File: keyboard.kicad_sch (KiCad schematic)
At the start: 1 part

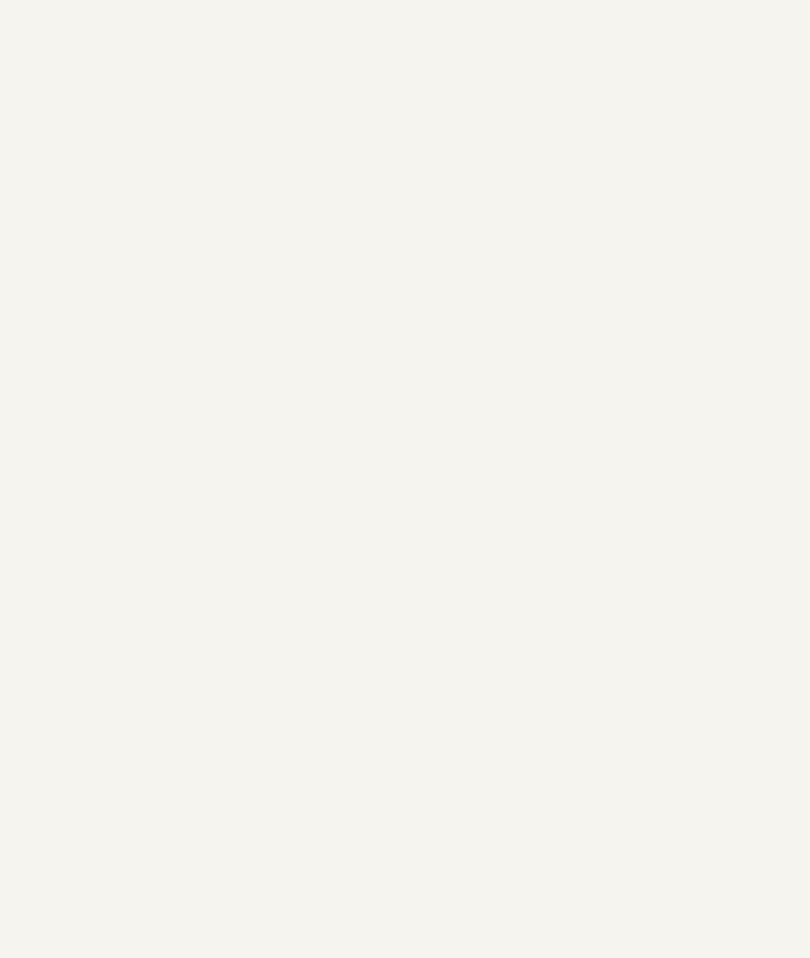
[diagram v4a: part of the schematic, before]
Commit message: added new stm uc
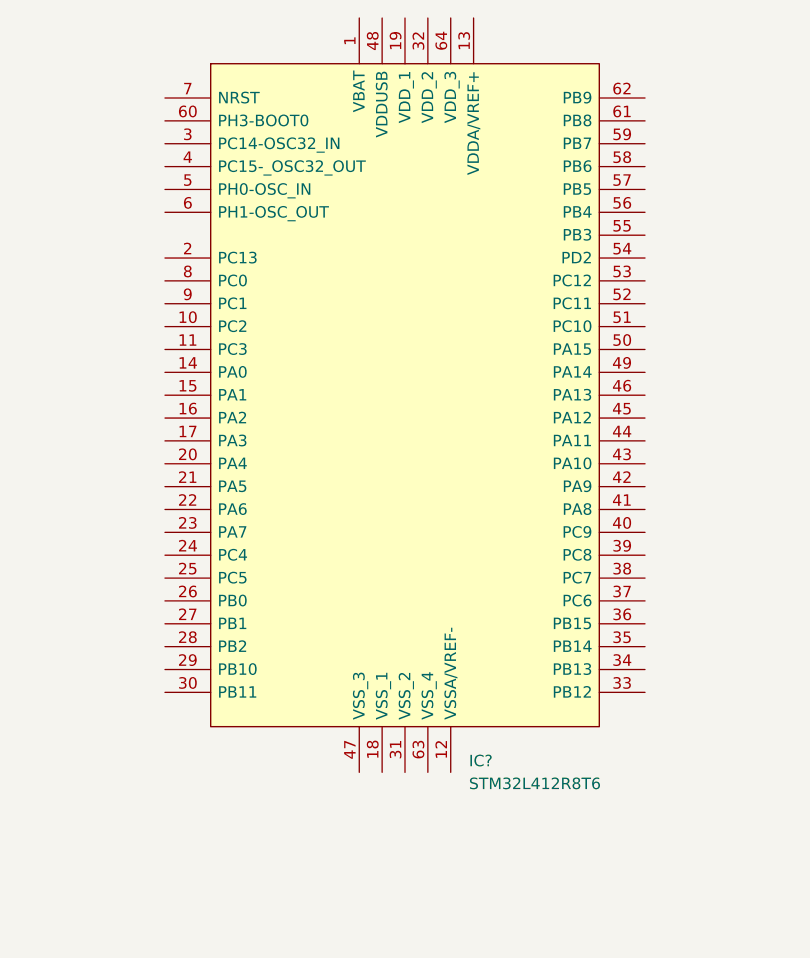
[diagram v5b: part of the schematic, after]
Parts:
- added IC?: STM32L412R8T6, CustomKeyboard:QFP50P1200X1200X160-64N, symbol CustomKeyboard:STM32L412R8T6
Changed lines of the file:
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@@
     (pin "1")
+  )
+  (symbol (lib_id "CustomKeyboard:STM32L412R8T6") (at 116.84 -74.93 0) (unit 1)
+    (in_bom yes) (on_board yes) (fields_autoplaced)
+    (property "Reference" "IC?" (id 0) (at 150.6094 -13.97 0)
+      (effects (font (size 1.27 1.27)) (justify left))
+    )
+    (property "Value" "STM32L412R8T6" (id 1) (at 150.6094 -11.43 0)
+      (effects (font (size 1.27 1.27)) (justify left))
+    )
+    (property "Footprint" "CustomKeyboard:QFP50P1200X1200X160-64N" (id 2) (at 166.37 -86.995 0)
+      (effects (font (size 1.27 1.27)) (justify left) hide)
+    )
+    (property "Datasheet" "https://www.st.com/resource/en/datasheet/stm32l412r8.pdf" (id 3) (at 166.37 -87.63 0)
+      (effects (font (size 1.27 1.27)) (justify left) hide)
+    )
+    (property "Description" "STMICROELECTRONICS - STM32L412R8T6 - MCU, 32BIT, 80MHZ" (id 4) (at 166.37 -85.09 0)
+      (effects (font (size 1.27 1.27)) (justify left) hide)
+    )
+    (property "Height" "1.6" (id 5) (at 166.37 -79.375 0)
+      (effects (font (size 1.27 1.27)) (justify left) hide)
+    )
+    (property "Mouser Part Number" "511-STM32L412R8T6" (id 6) (at 166.37 -76.835 0)
+      (effects (font (size 1.27 1.27)) (justify left) hide)
+    )
+    (property "Mouser Price/Stock" "https://www.mouser.co.uk/ProductDetail/STMicroelectronics/STM32L412R8T6?qs=l7cgNqFNU1ir0TjKK2zizg%3D%3D" (id 7) (at 166.37 -77.47 0)
+      (effects (font (size 1.27 1.27)) (justify left) hide)
+    )
+    (property "Manufacturer_Name" "STMicroelectronics" (id 8) (at 166.37 -71.755 0)
+      (effects (font (size 1.27 1.27)) (justify left) hide)
+    )
+    (property "Manufacturer_Part_Number" "STM32L412R8T6" (id 9) (at 166.37 -69.215 0)
+      (effects (font (size 1.27 1.27)) (justify left) hide)
+    )
+    (pin "1")
+    (pin "10")
+    (pin "11")
+    (pin "12")
+    (pin "13")
+    (pin "14")
+    (pin "15")
+    (pin "16")
+    (pin "17")
+    (pin "18")
+    (pin "19")
+    (pin "2")
+    (pin "20")
+    (pin "21")
+    (pin "22")
+    (pin "23")
+    (pin "24")
+    (pin "25")
+    (pin "26")
+    (pin "27")
+    (pin "28")
+    (pin "29")
+    (pin "3")
+    (pin "30")
+    (pin "31")
+    (pin "32")
+    (pin "33")
+    (pin "34")
+    (pin "35")
+    (pin "36")
+    (pin "37")
+    (pin "38")
+    (pin "39")
+    (pin "4")
+    (pin "40")
+    (pin "41")
+    (pin "42")
+    (pin "43")
+    (pin "44")
+    (pin "45")
+    (pin "46")
+    (pin "47")
+    (pin "48")
+    (pin "49")
+    (pin "5")
+    (pin "50")
+    (pin "51")
+    (pin "52")
+    (pin "53")
+    (pin "54")
+    (pin "55")
+    (pin "56")
+    (pin "57")
+    (pin "58")
+    (pin "59")
+    (pin "6")
+    (pin "60")
+    (pin "61")
+    (pin "62")
+    (pin "63")
+    (pin "64")
+    (pin "7")
+    (pin "8")
+    (pin "9")
   )
   (symbol (lib_id "power:VDDA") (at 137.16 55.88 0) (unit 1)
@@
       (reference "FB?") (unit 1) (value "FerriteBead_Small") (footprint "")
     )
+    (path "/89980449-61ca-4d0d-bed7-f5ec2ca07999"
+      (reference "IC?") (unit 1) (value "STM32L412R8T6") (footprint "CustomKeyboard:QFP50P1200X1200X160-64N")
+    )
     (path "/d6bc73ca-70ba-439e-a321-3561eb19c52a"

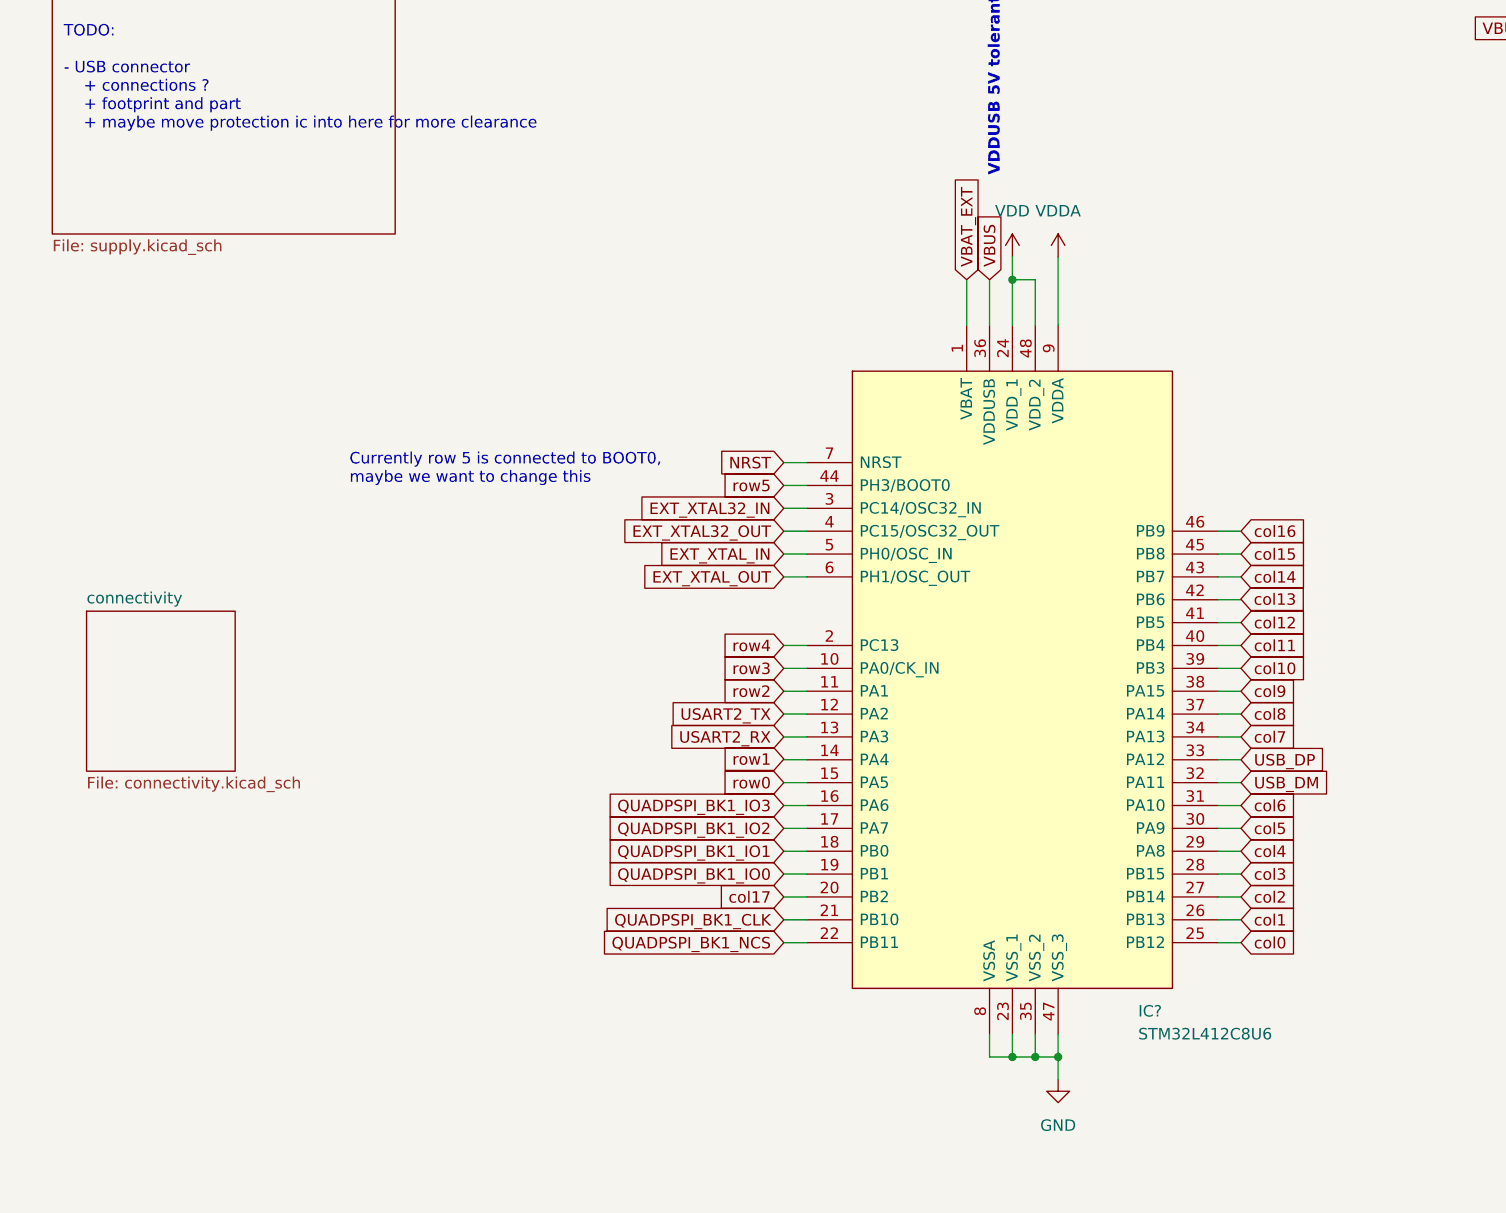
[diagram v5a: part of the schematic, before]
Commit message: Added wiring for new mcu
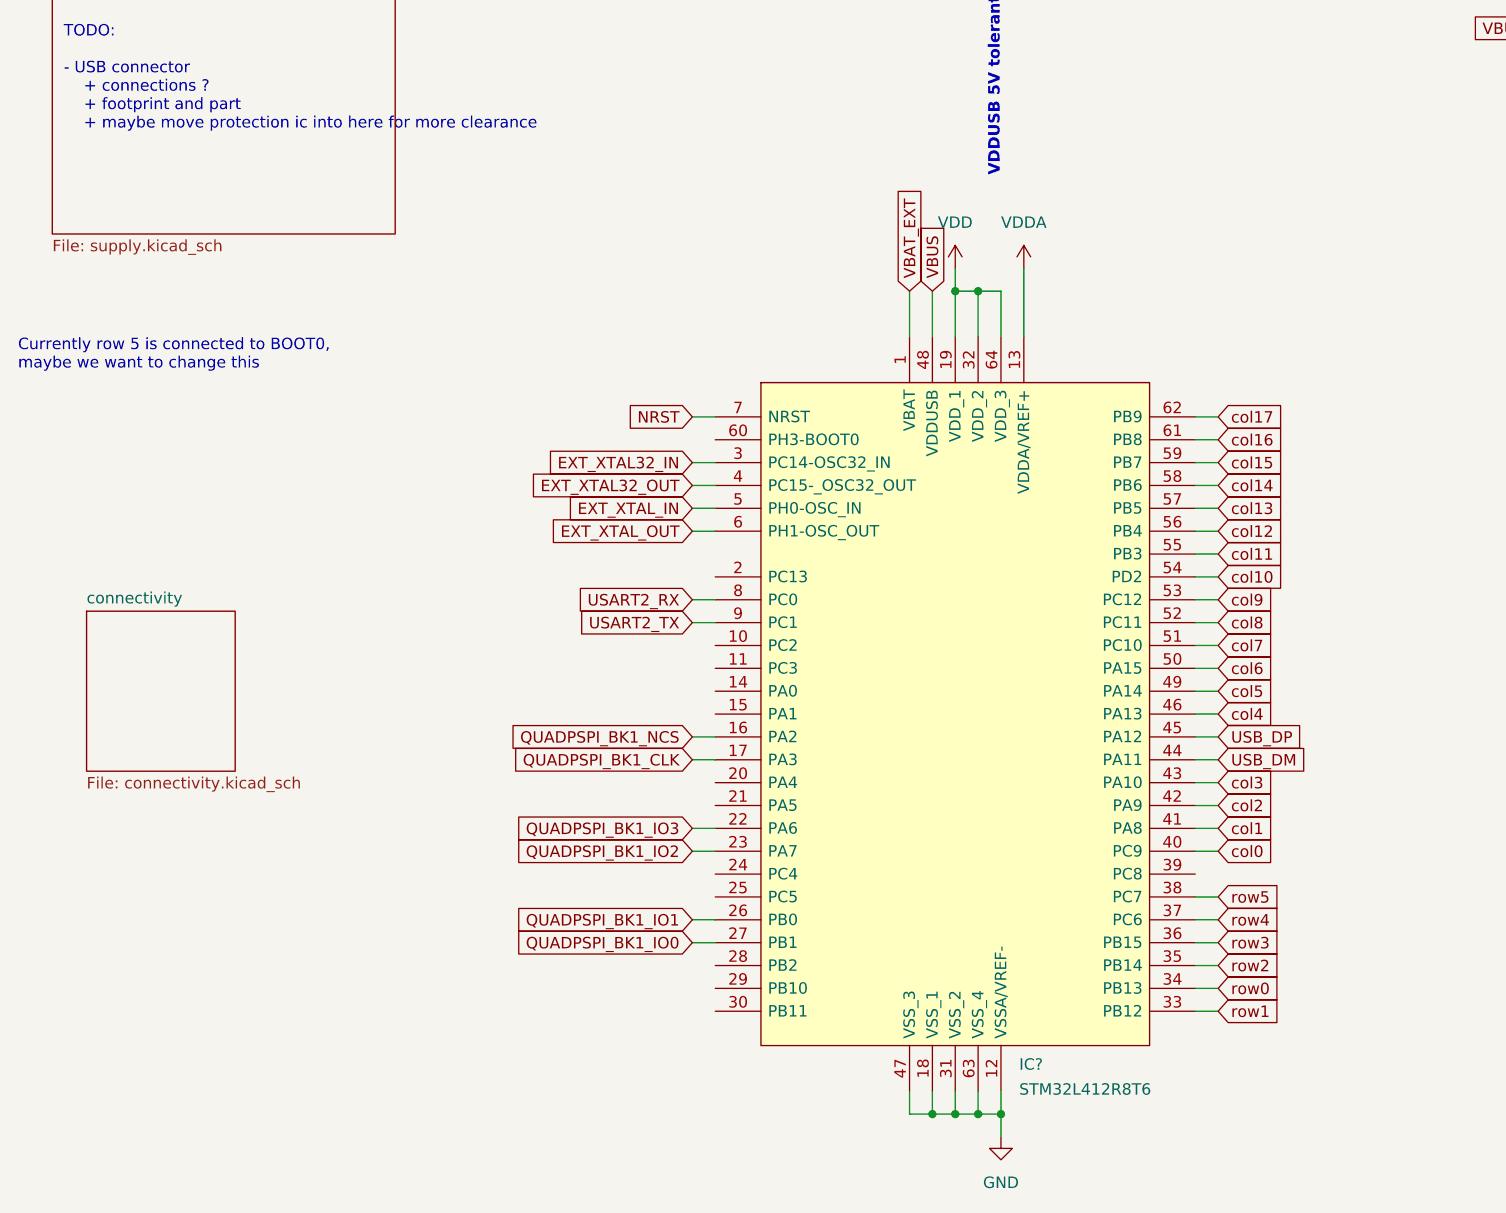
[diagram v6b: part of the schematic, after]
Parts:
- removed IC?: STM32L412C8U6, CustomKeyboard:QFN50P700X700X65-49N-D, symbol CustomKeyboard:STM32L412C8U6
- added IC?: STM32L412R8T6, CustomKeyboard:QFP50P1200X1200X160-64N, symbol CustomKeyboard:STM32L412R8T6
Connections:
- net EXT_XTAL32_IN: now also IC?.3 (PC14-OSC32_IN)
- net EXT_XTAL32_OUT: now also IC?.4 (PC15-_OSC32_OUT)
- net EXT_XTAL_IN: now also IC?.5 (PH0-OSC_IN)
- net EXT_XTAL_OUT: now also IC?.6 (PH1-OSC_OUT)
- net GND: now also IC?.12 (VSSA/VREF-), IC?.18 (VSS_1), IC?.31 (VSS_2), IC?.47 (VSS_3), IC?.63 (VSS_4)
- net NRST: now also IC?.7 (NRST)
- net QUADPSPI_BK1_CLK: now also IC?.17 (PA3)
- net QUADPSPI_BK1_IO0: now also IC?.27 (PB1)
- net QUADPSPI_BK1_IO1: now also IC?.26 (PB0)
- net QUADPSPI_BK1_IO2: now also IC?.23 (PA7)
- net QUADPSPI_BK1_IO3: now also IC?.22 (PA6)
- net QUADPSPI_BK1_NCS: now also IC?.16 (PA2)
- net USART2_RX: now also IC?.8 (PC0)
- net USART2_TX: now also IC?.9 (PC1)
- net USB_DM: now also IC?.44 (PA11)
- net USB_DP: now also IC?.45 (PA12)
- net VBAT_EXT: now also IC?.1 (VBAT)
- net VBUS: now also IC?.48 (VDDUSB)
- net VDD: now also IC?.19 (VDD_1), IC?.32 (VDD_2), IC?.64 (VDD_3)
- net VDDA: now also IC?.13 (VDDA/VREF+)
- net col0: now also IC?.40 (PC9)
- net col1: now also IC?.41 (PA8)
- net col10: now also IC?.54 (PD2)
- net col11: now also IC?.55 (PB3)
- net col12: now also IC?.56 (PB4)
- net col13: now also IC?.57 (PB5)
- net col14: now also IC?.58 (PB6)
- net col15: now also IC?.59 (PB7)
- net col16: now also IC?.61 (PB8)
- net col17: now also IC?.62 (PB9)
- net col2: now also IC?.42 (PA9)
- net col3: now also IC?.43 (PA10)
- net col4: now also IC?.46 (PA13)
- net col5: now also IC?.49 (PA14)
- net col6: now also IC?.50 (PA15)
- net col7: now also IC?.51 (PC10)
- net col8: now also IC?.52 (PC11)
- net col9: now also IC?.53 (PC12)
- net row0: now also IC?.34 (PB13)
- net row1: now also IC?.33 (PB12)
- net row2: now also IC?.35 (PB14)
- net row3: now also IC?.36 (PB15)
- net row4: now also IC?.37 (PC6)
- net row5: now also IC?.38 (PC7)
